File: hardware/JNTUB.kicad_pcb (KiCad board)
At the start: 2 copper layers, 70.6 x 128.5 mm, 67 parts, among them J1 PARAM1_CV, J10 B2_HDR_LEFT, J11 B2_HDR_RIGHT, J2 PARAM2_CV, J3 CLK/TRG, J4 DITTO, J5 OUT1, J6 OUT2, J7 B1_HDR_LEFT, J8 B1_HDR_RIGHT, J9 POWER, Q1 2N3904, Q2 2N3904, Q3 2N3904, U1 ATtiny85, U2 TL074, U3 78L05, U4 79L05

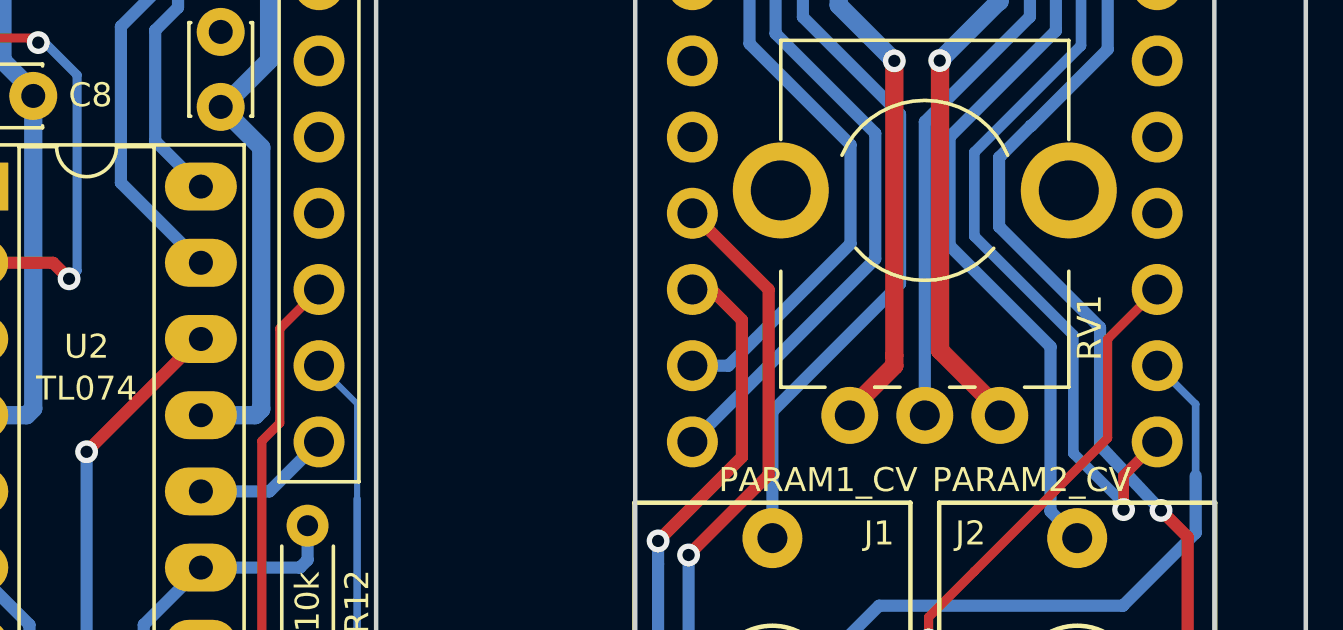
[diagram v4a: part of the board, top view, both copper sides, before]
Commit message: [JNTUB-HW] Clean up straggling traces
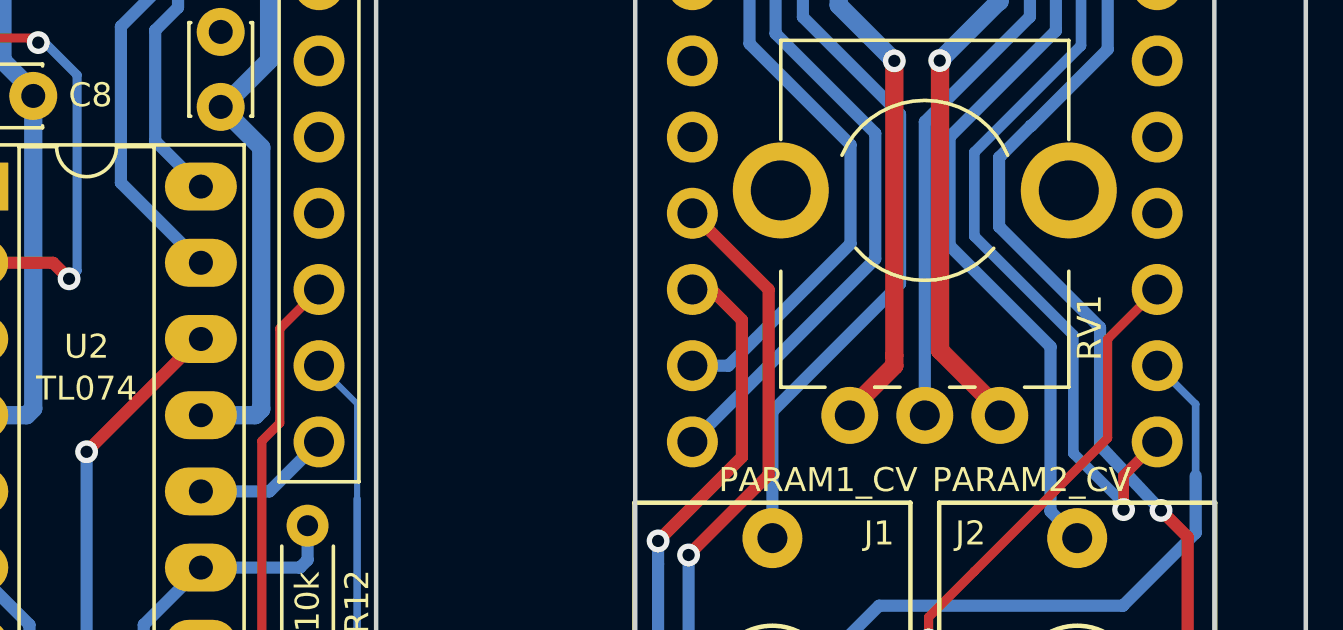
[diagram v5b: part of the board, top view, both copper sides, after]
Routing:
- net /PeripheralBoard/P3_POT: track 58.8 -> 58.1 mm
- net Net-(JP1-Pad1): track 36.6 -> 36.0 mm
- net /PeripheralBoard/IN_LED+: track 26.0 -> 25.5 mm
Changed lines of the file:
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@@
     (thickness 1.6)
     (drawings 161)
-    (tracks 549)
+    (tracks 545)
     (zones 0)
     (modules 67)
@@
   (layers
     (0 F.Cu signal)
-    (31 B.Cu signal)
+    (31 B.Cu signal hide)
     (32 B.Adhes user)
     (33 F.Adhes user)
@@
   (segment (start 212.471 83.439) (end 213.487 83.439) (width 0.4064) (layer F.Cu) (net 16))
   (segment (start 209.650132 80.618132) (end 212.471 83.439) (width 0.4064) (layer F.Cu) (net 16))
-  (segment (start 209.55 101.473) (end 209.0058 101.473) (width 0.3048) (layer F.Cu) (net 16))
-  (segment (start 209.55 101.473) (end 209.4738 101.473) (width 0.3048) (layer F.Cu) (net 16))
   (segment (start 205.486 83.185) (end 205.486 83.6295) (width 0.3048) (layer F.Cu) (net 16))
   (segment (start 203.327 81.026) (end 205.486 83.185) (width 0.3048) (layer F.Cu) (net 16))
@@
   (segment (start 233.807 114.046) (end 233.807 122.301) (width 0.4064) (layer B.Cu) (net 30))
   (via (at 233.807 114.046) (size 0.762) (drill 0.4064) (layers F.Cu B.Cu) (net 30))
-  (segment (start 241.427 102.362) (end 241.427 102.892158) (width 0.4064) (layer F.Cu) (net 30))
   (segment (start 237.998 109.093) (end 235.331 111.76) (width 0.3048) (layer F.Cu) (net 30))
   (segment (start 241.427 102.362) (end 239.776 104.013) (width 0.3048) (layer F.Cu) (net 30))
@@
   (segment (start 239.776 89.027) (end 241.427 87.351422) (width 0.4064) (layer B.Cu) (net 35))
   (segment (start 239.776 94.361) (end 239.776 89.027) (width 0.4064) (layer B.Cu) (net 35))
-  (segment (start 225.933 104.902) (end 226.568 104.902) (width 0.4064) (layer F.Cu) (net 36))
   (segment (start 227.838 85.852) (end 224.79 82.804) (width 0.4064) (layer B.Cu) (net 36))
   (segment (start 233.676799 64.258799) (end 233.68 64.262) (width 0.4064) (layer B.Cu) (net 36))

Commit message: [JNTUB-HW] Add JLCPCB note for part number
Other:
- board text added: "JLCJLCJLCJLC"
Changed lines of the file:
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@@
   (general
     (thickness 1.6)
-    (drawings 161)
+    (drawings 163)
     (tracks 545)
     (zones 0)
@@
   (layers
     (0 F.Cu signal)
-    (31 B.Cu signal hide)
+    (31 B.Cu signal)
     (32 B.Adhes user)
     (33 F.Adhes user)
@@
     (46 B.CrtYd user)
     (47 F.CrtYd user)
-    (48 B.Fab user)
-    (49 F.Fab user)
+    (48 B.Fab user hide)
+    (49 F.Fab user hide)
   )
   (setup
@@
     (visible_elements FFFFFF7F)
     (pcbplotparams
-      (layerselection 0x00030_80000001)
+      (layerselection 0x010f0_ffffffff)
       (usegerberextensions false)
       (usegerberattributes true)
@@
       (outputformat 1)
       (mirror false)
-      (drillshape 1)
+      (drillshape 0)
       (scaleselection 1)
       (outputdirectory ""))
@@
     )
   )
+  (gr_text JLCJLCJLCJLC (at 241.554 145.034 90) (layer B.SilkS)
+    (effects (font (size 0.8 0.8) (thickness 0.15)) (justify left mirror))
+  )
+  (gr_text JLCJLCJLCJLC (at 211.074 147.066 90) (layer B.SilkS)
+    (effects (font (size 0.8 0.8) (thickness 0.15)) (justify left mirror))
+  )
   (gr_text "Board 1 of 2" (at 235.077 145.796 90) (layer B.SilkS)

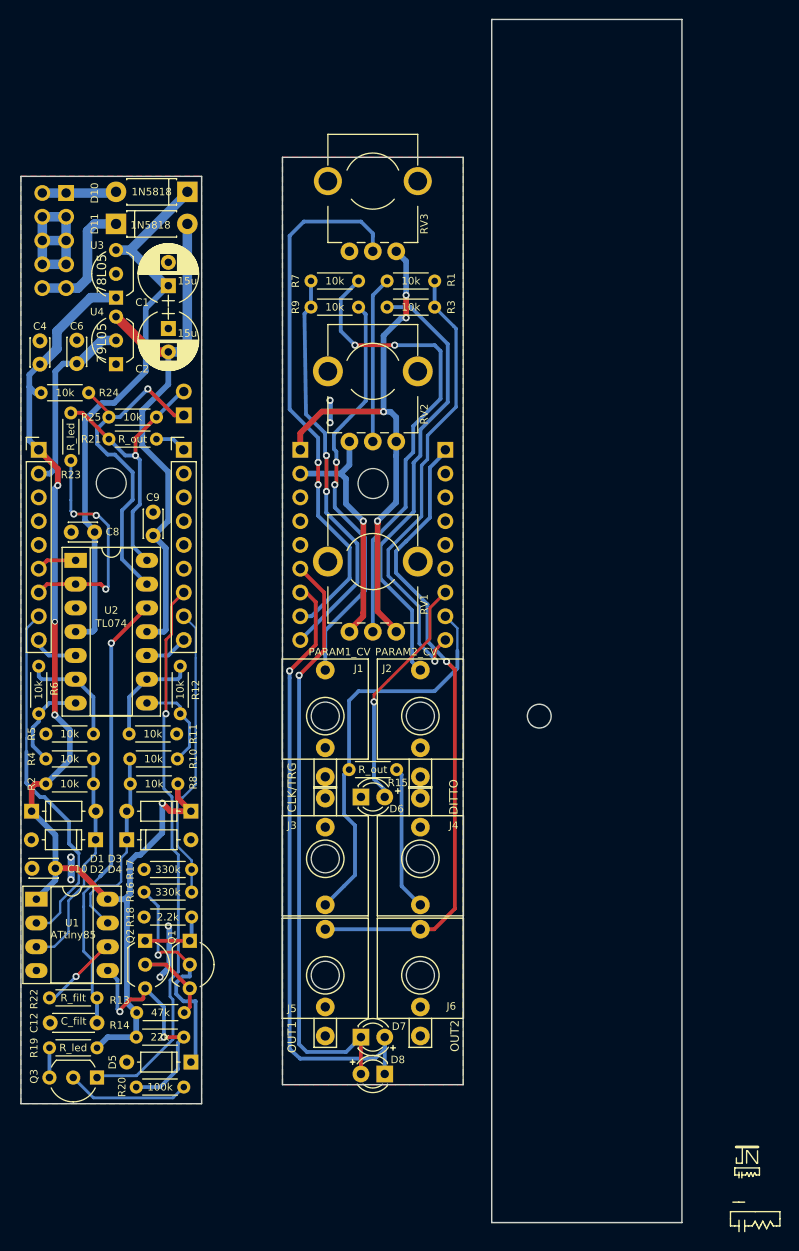
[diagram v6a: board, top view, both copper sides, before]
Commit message: [JNTUB-HW] Move front panel to separate PCB file
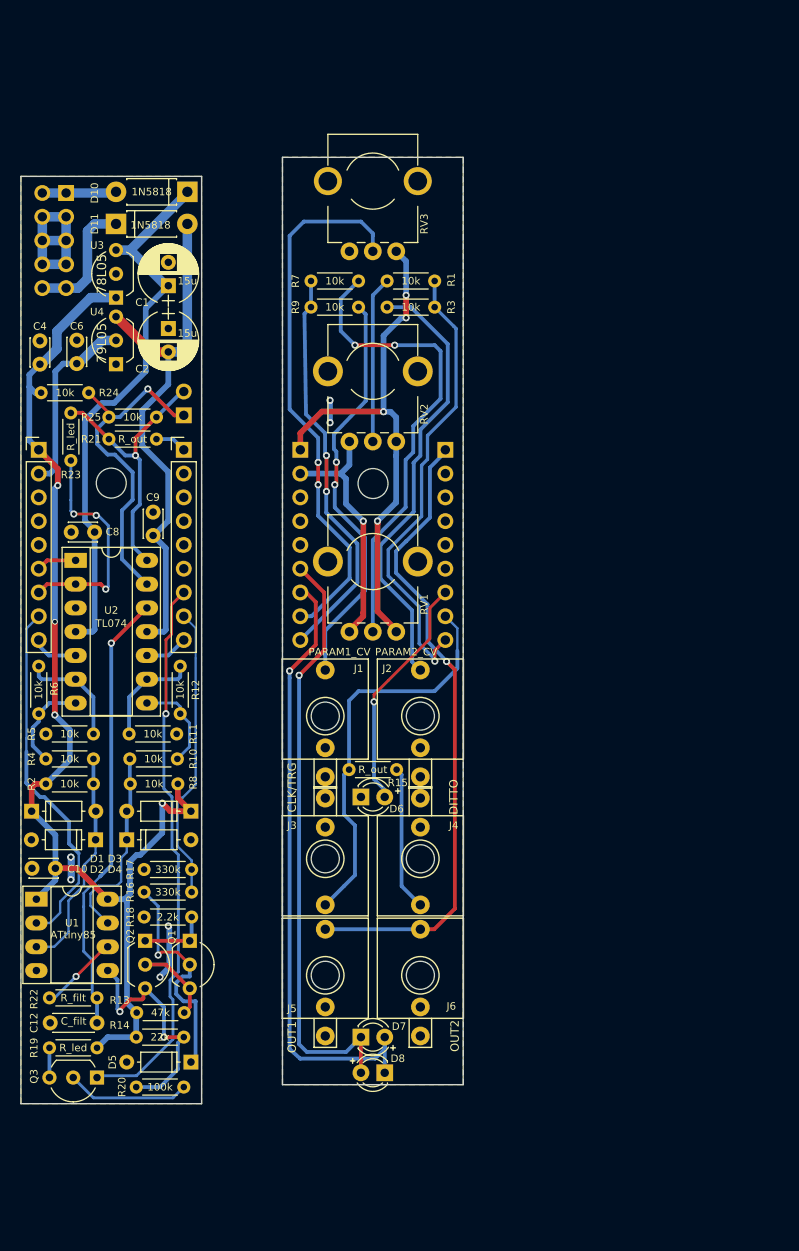
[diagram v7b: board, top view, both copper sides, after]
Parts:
- moved D8 0.13 mm to (234.9, 153.7)
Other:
- board size 70.6 x 128.5 mm -> 47.2 x 101.1 mm

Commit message: [JNTUB-HW] JNTUB Hardware Revision 0.2
* Add resistor to drain C12 (PWM filter cap)
* Add optional parallel resistor to PWM filter
  * selectable by jumper
  * increases the cutoff frequency to audio range
* Add resistor between 5V and MCU RESET to allow for ISP
* Move a few resistors to Board 1
* Add ISP programming headers!
* Change all resistors and diodes to standing
* Shorten pin headers that connect Boards 1 and 2
* Ditch ground pour on Board 1 in favor of direct traces
* Move CV 1 and CV 2 jacks down a bit
* Slightly adjust LED positions
* Adjust front panel to match moved components
* Tweak design of front panel
* Fix up some 3D models
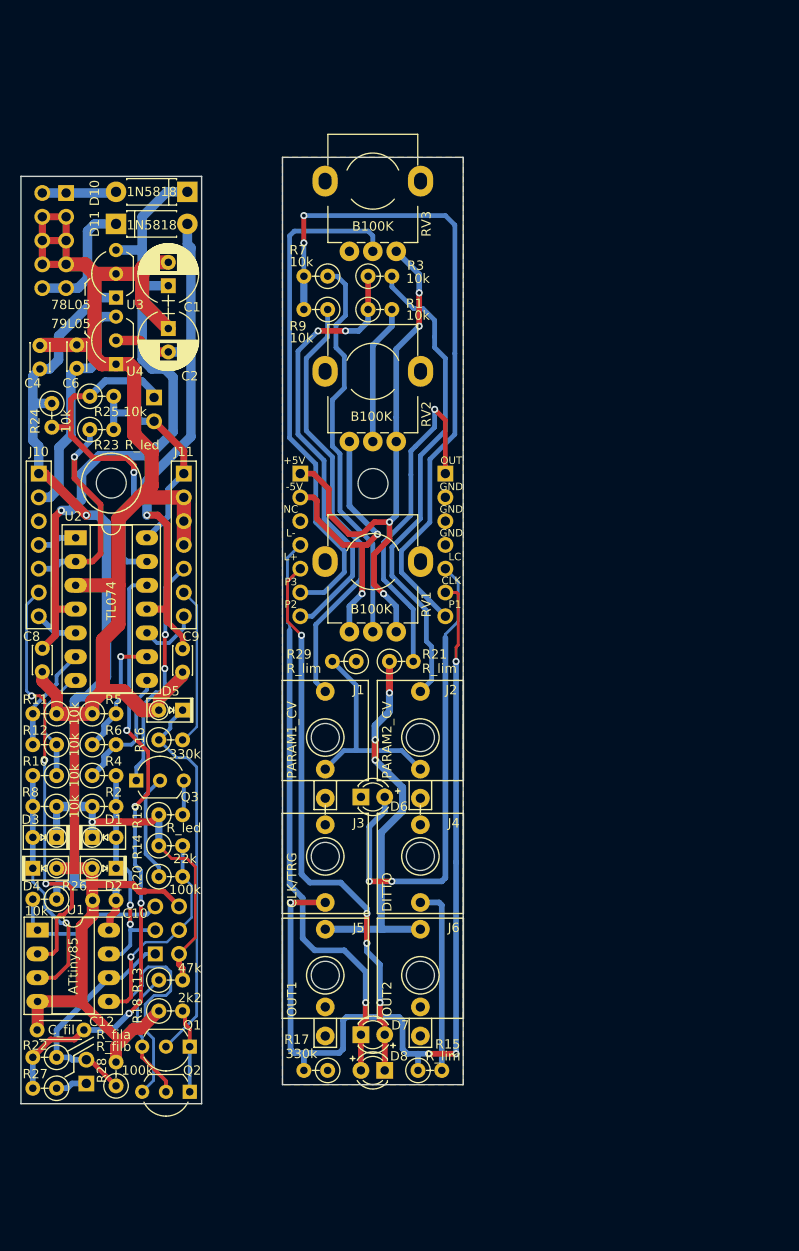
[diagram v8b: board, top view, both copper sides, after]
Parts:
- added J12: ISP, Pin_Headers:Pin_Header_Straight_2x03_Pitch2.54mm, B.Cu at (210.4, 141.0)
- added JP2: JMP_AUDIO, Pin_Headers:Pin_Header_Straight_1x02_Pitch2.54mm, B.Cu at (203.1, 154.8)
- added R26: 10k, SDIY:R_Axial_DIN0207_L6.3mm_D2.5mm_P2.54mm_Vertical, F.Cu at (199.9, 135.1)
- added R27: R_filb, SDIY:R_Axial_DIN0207_L6.3mm_D2.5mm_P2.54mm_Vertical, F.Cu at (199.9, 155.3)
- added R28: 100k, SDIY:R_Axial_DIN0207_L6.3mm_D2.5mm_P2.54mm_Vertical, F.Cu at (206.2, 155.1)
- added R29: R_lim, SDIY:R_Axial_DIN0207_L6.3mm_D2.5mm_P2.54mm_Vertical, F.Cu at (231.9, 109.7)
- C12: value C_filt -> C_fil
- D1, D3: footprint SDIY:D_DO-35_SOD27_P6.85mm_Horizontal -> SDIY:D_DO-35_SOD27_P2.54mm_Vertical_AnodeUp
- D2, D4, D5: footprint SDIY:D_DO-35_SOD27_P6.85mm_Horizontal -> SDIY:D_DO-35_SOD27_P2.54mm_Vertical_KathodeUp
- D6: value IN_LED -> CLK_LED
- D7: value OUT_LED+ -> LED_POS
- D8: value OUT_LED- -> LED_NEG
- J1, J2, J5, J6: footprint SDIY:PJ301M-12 -> SDIY:PJ301M-12_Thonkiconn
- J10, J11, J7, J8: footprint Pin_Headers:Pin_Header_Straight_1x09_Pitch2.54mm -> Pin_Headers:Pin_Header_Straight_1x07_Pitch2.54mm
- J3, J4: footprint SDIY:PJ301M-12 -> SDIY:PJ301M-12_Thonkiconn_NoGround
- R1, R10, R11, R12, R13, R14, R16, R17, R19, R2, R20, R23, R24, R25, R3, R4, R5, R6, R7, R8, R9: footprint SDIY:R_Axial_DIN0204_L3.6mm_D1.6mm_P5.08mm_Horizontal -> SDIY:R_Axial_DIN0207_L6.3mm_D2.5mm_P2.54mm_Vertical
- R15, R21: value R_out -> R_lim; footprint SDIY:R_Axial_DIN0204_L3.6mm_D1.6mm_P5.08mm_Horizontal -> SDIY:R_Axial_DIN0207_L6.3mm_D2.5mm_P2.54mm_Vertical
- R18: value 2.2k -> 2k2; footprint SDIY:R_Axial_DIN0204_L3.6mm_D1.6mm_P5.08mm_Horizontal -> SDIY:R_Axial_DIN0207_L6.3mm_D2.5mm_P2.54mm_Vertical
- R22: value R_filt -> R_fila; footprint SDIY:R_Axial_DIN0204_L3.6mm_D1.6mm_P5.08mm_Horizontal -> SDIY:R_Axial_DIN0207_L6.3mm_D2.5mm_P2.54mm_Vertical
- moved D5 37.6 mm to (213.4, 114.9)
- moved R21 34.4 mm to (235.5, 109.7), turned to 0 degrees
- moved R15 32.2 mm to (238.5, 153.4), turned to 0 degrees
- moved Q3 32.0 mm to (208.4, 122.5), turned to 0 degrees
- moved R17 29.1 mm to (228.9, 153.4), turned to 180 degrees
- moved R19 27.5 mm to (210.8, 126.1)
- moved R20 22.6 mm to (210.8, 132.7), turned to 0 degrees
- moved R14 20.6 mm to (210.8, 129.4), turned to 0 degrees
- moved C9 17.4 mm to (213.4, 110.9), turned to 90 degrees
- moved Q2 16.8 mm to (214.1, 155.7), turned to 180 degrees
- moved R16 16.3 mm to (210.8, 118.1)
- moved D3 14.6 mm to (199.9, 128.5)
- moved C8 13.6 mm to (198.4, 108.3), turned to 270 degrees
- moved R12 13.6 mm to (199.9, 118.6), turned to 180 degrees
- moved R8 13.2 mm to (199.9, 125.2)
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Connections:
- D1 pad 2: /MainBoard/MCU_ADC2 -> /MainBoard/MCU_ADC1
- D2 pad 1: /MainBoard/MCU_ADC2 -> /MainBoard/MCU_ADC1
- D3 pad 2: /MainBoard/MCU_ADC1 -> /MainBoard/MCU_ADC2
- D4 pad 1: /MainBoard/MCU_ADC1 -> /MainBoard/MCU_ADC2
- D6 pad 2: /PeripheralBoard/IN_LED+ -> /PeripheralBoard/CLK_LED
- D7 pad 1: /PeripheralBoard/OUT_LED- -> /PeripheralBoard/LED_NEG
- D7 pad 2: /PeripheralBoard/OUT_LED+ -> /PeripheralBoard/LED_POS
- D8 pad 1: /PeripheralBoard/OUT_LED+ -> /PeripheralBoard/LED_POS
- D8 pad 2: /PeripheralBoard/OUT_LED- -> /PeripheralBoard/LED_NEG
- J10 pad 3: GNDREF -> Net-(J10-Pad3)
- J10 pad 4: GNDREF -> /MainBoard/LED_NEG
- J10 pad 5: GNDREF -> /MainBoard/LED_POS
- J10 pad 6: /MainBoard/OUT_LED- -> /MainBoard/MCU_ADC3
- J10 pad 7: /MainBoard/OUT_LED+ -> /MainBoard/P2_AVG
- J11 pad 5: GNDREF -> /MainBoard/CLK_LED
- J11 pad 6: GNDREF -> /MainBoard/CLK_TRG
- J11 pad 7: /MainBoard/IN_LED+ -> /MainBoard/P1_AVG
- J2 pad 2: Net-(J2-Pad2) -> Net-(J1-Pad2)
- J4 pad 3: Net-(J4-Pad3) -> /PeripheralBoard/DITTO
- J5 pad 3: /PeripheralBoard/OUT -> /PeripheralBoard/OUT1
- J6 pad 3: /PeripheralBoard/OUT -> /PeripheralBoard/OUT1
- J7 pad 3: GNDREF -> Net-(J7-Pad3)
- J7 pad 4: GNDREF -> /PeripheralBoard/LED_NEG
- J7 pad 5: GNDREF -> /PeripheralBoard/LED_POS
- J7 pad 6: /PeripheralBoard/OUT_LED- -> /PeripheralBoard/P3_POT
- J7 pad 7: /PeripheralBoard/OUT_LED+ -> /PeripheralBoard/P2_AVG
- J8 pad 5: GNDREF -> /PeripheralBoard/CLK_LED
- J8 pad 6: GNDREF -> /PeripheralBoard/CLK_TRG
- J8 pad 7: /PeripheralBoard/IN_LED+ -> /PeripheralBoard/P1_AVG
- JP1 pad 2: Net-(JP1-Pad2) -> /MainBoard/OUT
- Q3 pad 1: /MainBoard/IN_LED+ -> /MainBoard/CLK_LED
- R1 pad 1: /PeripheralBoard/P2_POT -> /PeripheralBoard/P2_AVG
- R1 pad 2: /PeripheralBoard/P2_AVG -> /PeripheralBoard/P2_POT
- R10 pad 2: /MainBoard/MCU_ADC1 -> /MainBoard/MCU_ADC2
- R11 pad 1: Net-(R11-Pad1) -> GNDREF
- R11 pad 2: GNDREF -> Net-(R11-Pad2)
- R12 pad 2: Net-(R11-Pad1) -> Net-(R11-Pad2)
- R14 pad 1: /MainBoard/MCU_PB0 -> +5V
- R14 pad 2: +5V -> /MainBoard/MCU_PB0
- R15 pad 1: Net-(J4-Pad3) -> /PeripheralBoard/CLK_TRG
- R15 pad 2: /PeripheralBoard/CLK_TRG -> /PeripheralBoard/DITTO
- R17 pad 2: /MainBoard/CLK_TRG -> /PeripheralBoard/CLK_TRG
- R19 pad 1: Net-(Q3-Pad3) -> +5V
- R19 pad 2: +5V -> Net-(Q3-Pad3)
- R2 pad 2: /MainBoard/MCU_ADC2 -> /MainBoard/MCU_ADC1
- R21 pad 1: /MainBoard/OUT -> /PeripheralBoard/OUT1
- R21 pad 2: Net-(JP1-Pad2) -> /PeripheralBoard/OUT
- R23 pad 1: Net-(JP1-Pad2) -> /MainBoard/LED_POS
- R23 pad 2: /MainBoard/OUT_LED+ -> /MainBoard/OUT
- R25 pad 2: Net-(JP1-Pad2) -> /MainBoard/OUT
- R3 pad 1: /PeripheralBoard/P2_CV -> /PeripheralBoard/P2_AVG
- R3 pad 2: /PeripheralBoard/P2_AVG -> /PeripheralBoard/P2_CV
- R4 pad 2: /MainBoard/MCU_ADC2 -> /MainBoard/MCU_ADC1
- R5 pad 1: Net-(R5-Pad1) -> GNDREF
- R5 pad 2: GNDREF -> Net-(R5-Pad2)
- R6 pad 1: Net-(R4-Pad1) -> Net-(R5-Pad2)
- R6 pad 2: Net-(R5-Pad1) -> Net-(R4-Pad1)
- R8 pad 2: /MainBoard/MCU_ADC1 -> /MainBoard/MCU_ADC2
- U1 pad 1: +5V -> /MainBoard/MCU_RESET
- U2 pad 1: /MainBoard/OUT_LED- -> /MainBoard/LED_NEG
- U2 pad 10: /MainBoard/P2_AVG -> /MainBoard/P1_AVG
- U2 pad 14: Net-(JP1-Pad2) -> /MainBoard/OUT
- U2 pad 2: /MainBoard/OUT_LED+ -> /MainBoard/LED_POS
- U2 pad 5: /MainBoard/P1_AVG -> /MainBoard/P2_AVG
- U2 pad 6: Net-(R5-Pad1) -> Net-(R11-Pad2)
- U2 pad 7: Net-(R4-Pad1) -> Net-(R10-Pad1)
- U2 pad 8: Net-(R10-Pad1) -> Net-(R4-Pad1)
- U2 pad 9: Net-(R11-Pad1) -> Net-(R5-Pad2)
- U4 pad 2: -5V -> -12V
- U4 pad 3: -12V -> -5V
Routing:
- net GNDREF: track 25.9 -> 198.9 mm, vias 4 -> 0
- net /PeripheralBoard/OUT_LED+: track 68.7 -> 0.00 mm, vias 1 -> 0
- net /PeripheralBoard/OUT_LED-: track 65.0 -> 0.00 mm, vias 1 -> 0
- net /PeripheralBoard/LED_NEG: track 0.00 -> 62.2 mm, vias 0 -> 1
- net /PeripheralBoard/LED_POS: track 0.00 -> 60.9 mm, vias 0 -> 4
- net /MainBoard/IN_LED+: track 59.5 -> 0.00 mm, vias 1 -> 0
- net /PeripheralBoard/CLK_TRG: track 42.9 -> 98.3 mm, vias 0 -> 4
- net /PeripheralBoard/CLK_LED: track 0.00 -> 52.9 mm, vias 0 -> 2
- net /PeripheralBoard/OUT1: track 0.00 -> 41.6 mm, vias 0 -> 3
- net /PeripheralBoard/OUT: track 68.5 -> 37.8 mm
- net Net-(JP1-Pad2): track 30.2 -> 0.00 mm, vias 1 -> 0
- net /PeripheralBoard/P1_AVG: track 43.5 -> 72.4 mm
- net /PeripheralBoard/IN_LED+: track 25.5 -> 0.00 mm, vias 1 -> 0
- net /MainBoard/CLK_LED: track 0.00 -> 25.1 mm, vias 0 -> 2
- net /MainBoard/OUT_LED+: track 24.7 -> 0.00 mm, vias 3 -> 0
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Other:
- net class Ground added: clearance 0.508, trace_width 1.27, via_dia 1.016, via_drill 0.6096
- net class Power: clearance 0.508 -> 0.4064
- board text added: "+5V"
- board text added: "-5V"
- board text added: "CLK"
- board text added: "GND"
- board text added: "ISP"
- board text added: "Jan. 2021"
- board text added: "L+"
- board text added: "L-"
- board text added: "LC"
- board text added: "NC"
- board text added: "OUT"
- board text added: "P1"
- board text added: "P2"
- board text added: "P3"
- board text added: "Rev 0.2"
- board text added: "Set for audio OUT"
- board text removed: "Dec. 2020"
- board text removed: "Rev 0.1"
